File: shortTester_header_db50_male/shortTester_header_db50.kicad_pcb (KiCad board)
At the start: 2 copper layers, 40 x 123 mm, 2 parts, among them J1 Conn_02x38_Counter_Clockwise, J2 Conn_02x25_Counter_Clockwise

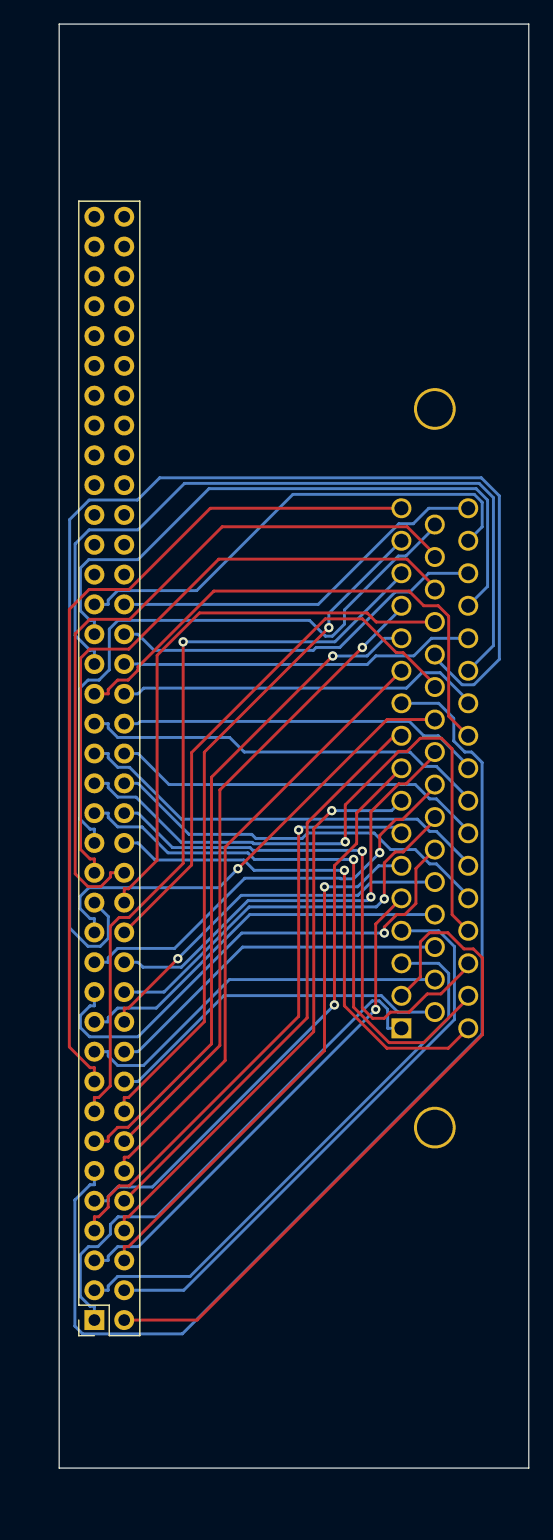
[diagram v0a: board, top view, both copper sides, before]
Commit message: Fixed missing tracks. Simplified MUx GND. Added software.
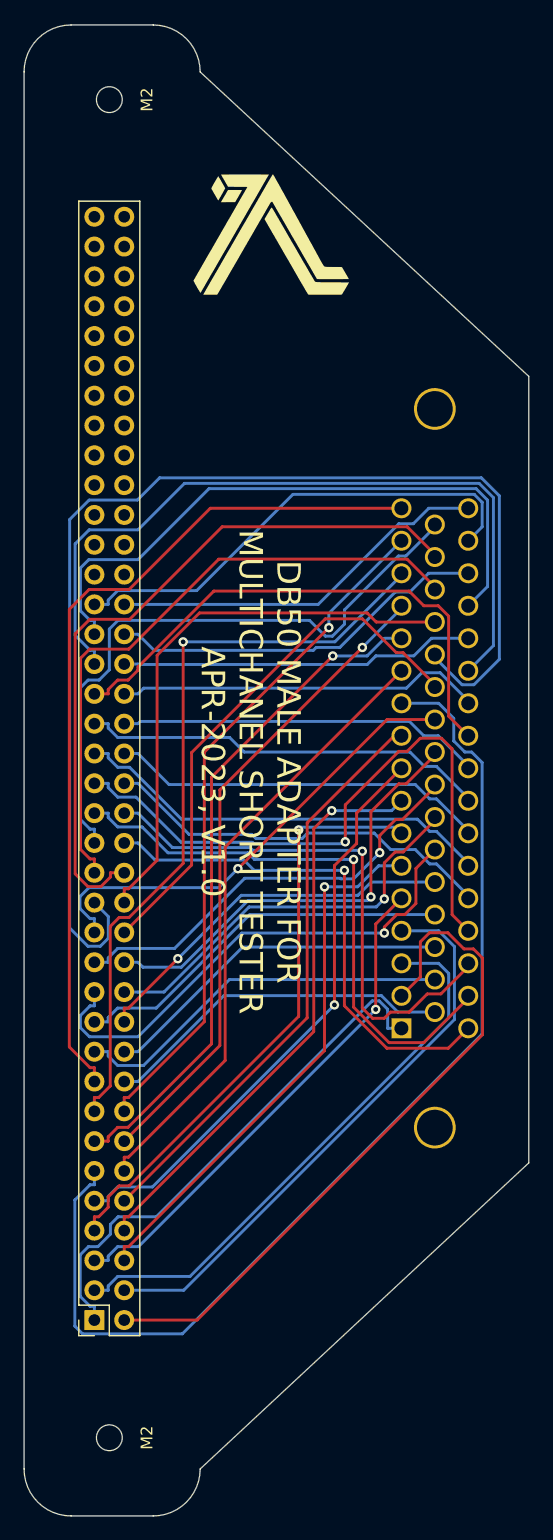
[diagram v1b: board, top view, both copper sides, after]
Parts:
- added G***: LOGO, skLib:lamda15mm, F.Cu at (119.0, 46.0)
- added G***: LOGO, skLib:lamda15mm, B.Cu at (119.0, 138.0)
- added M2: MountingHole_2.2mm_M2, MountingHole:MountingHole_2.2mm_M2, F.Cu at (105.3, 34.4)
- added M2: MountingHole_2.2mm_M2, MountingHole:MountingHole_2.2mm_M2, F.Cu at (105.3, 148.4)
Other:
- board size 40 x 123 mm -> 43 x 127 mm
- board text added: "DB50 MALE ADAPTER FOR MULTICHANEL SHORT TESTER APR-2023, V1.0"
